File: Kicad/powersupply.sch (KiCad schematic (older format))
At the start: 19 parts, among them J801 Jack 2/6.3mm, Q801 BC546, Q802 BC556, U801 DC-DC Module, U802 MAX1615, U803 TLV1117 3.3V 1A

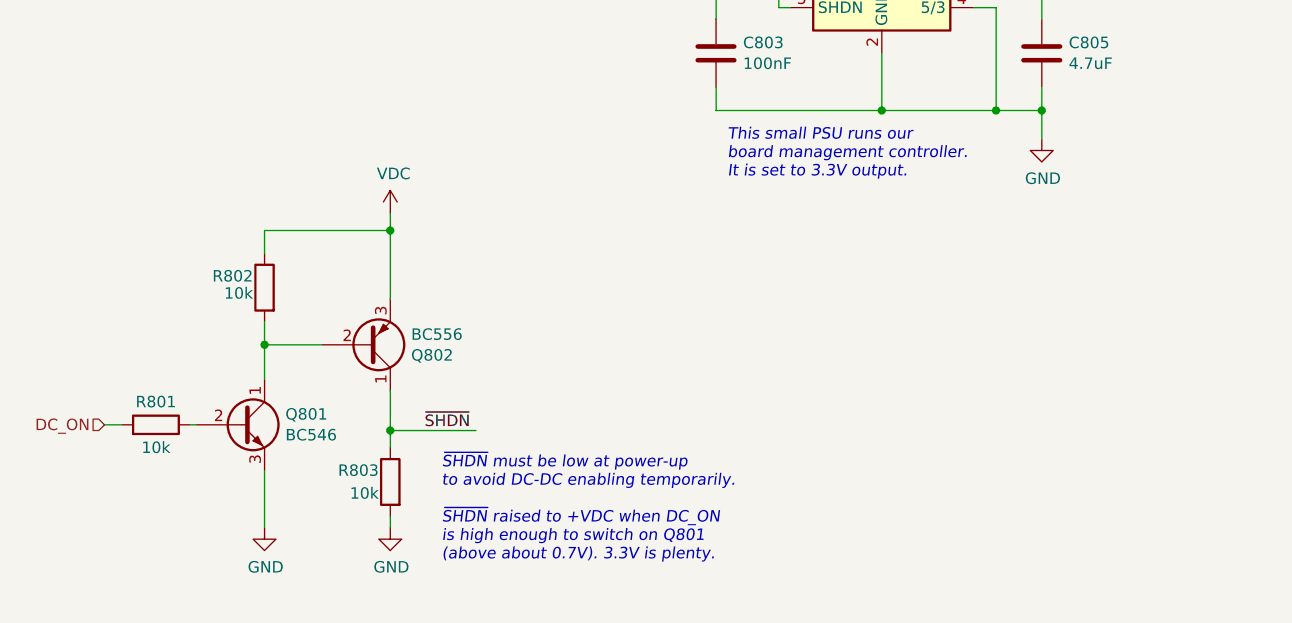
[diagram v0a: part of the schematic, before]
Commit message: Reworked DC-DC power-on circuit.
Base of Q802 doesn't need a pull-up.
Base of Q802 does need a current limiting resistor.

Swapped Q802 and Q801 on PCB to make routing simpler. Also
labelled which is PNP and which is NPN!
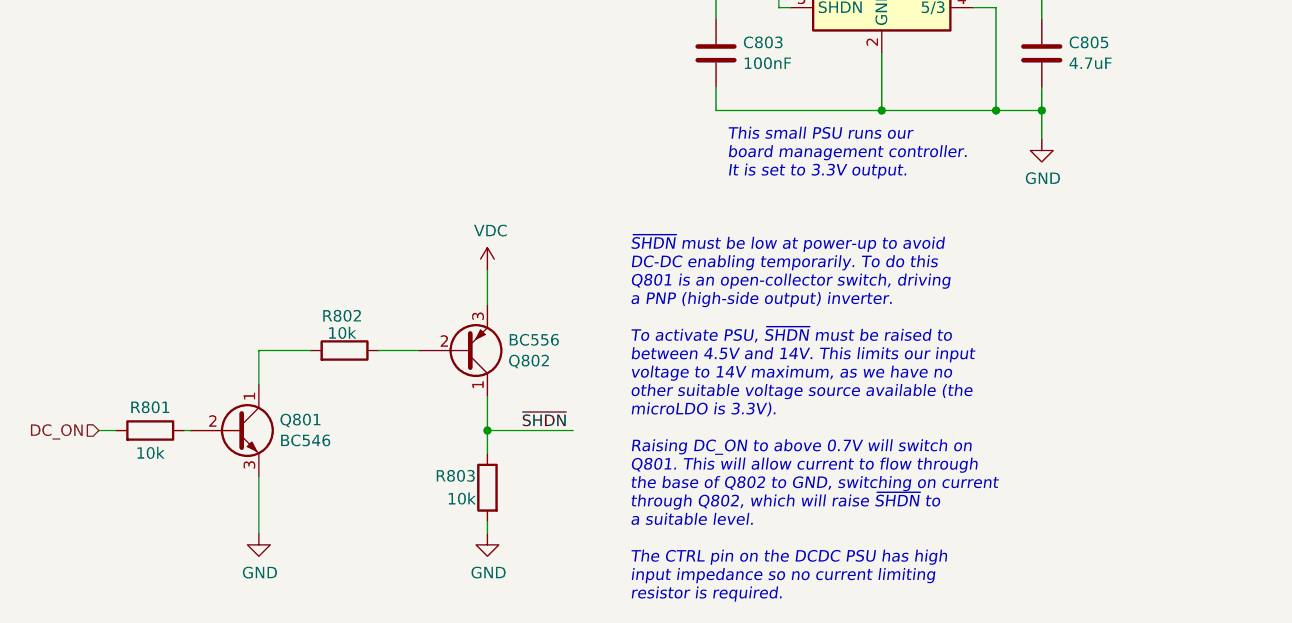
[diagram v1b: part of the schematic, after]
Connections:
- wire segments 66 -> 63
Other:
- note added: "~SHDN~ must be low at power-up to avoid\nDC-DC enabling temporarily. To do this\nQ801 is an open-collector switch, driving\na PNP (high-side output) inverter.\n\nTo activate PSU, ~SHDN~ must be raised to\nbetween 4.5V and 14V. This limits our input\nvoltage to 14V maximum, as we have no\nother suitable voltage source available (the\nmicroLDO is 3.3V).\n\nRaising DC_ON to above 0.7V will switch on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"
- note removed: "~SHDN~ must be low at power-up\nto avoid DC-DC enabling temporarily.\n\n~SHDN~ raised to +VDC when DC_ON\nis high enough to switch on Q801\n(above about 0.7V). 3.3V is plenty."
- moved on the sheet: Q801, Q802, R801, R802, R803

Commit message: Added expansion header.
Involved rerouting quite a few things.
Also added through-hole switches for power/reset.
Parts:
- renumbered C801 to C701, C802 to C702, C803 to C703, C804 to C704, C805 to C705, C808 to C706, C806 to C707, C807 to C708, F801 to F701, J801 to J701, L801 to L701, Q801 to Q701, Q802 to Q702, R801 to R701, R802 to R702, R803 to R703, U801 to U701, U802 to U702, U803 to U703
